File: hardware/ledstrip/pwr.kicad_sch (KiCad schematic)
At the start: 30 parts, among them J6 Header for STUSB4500 I2C, Q4 Q_PMOS, U6 STUSB4500QTR

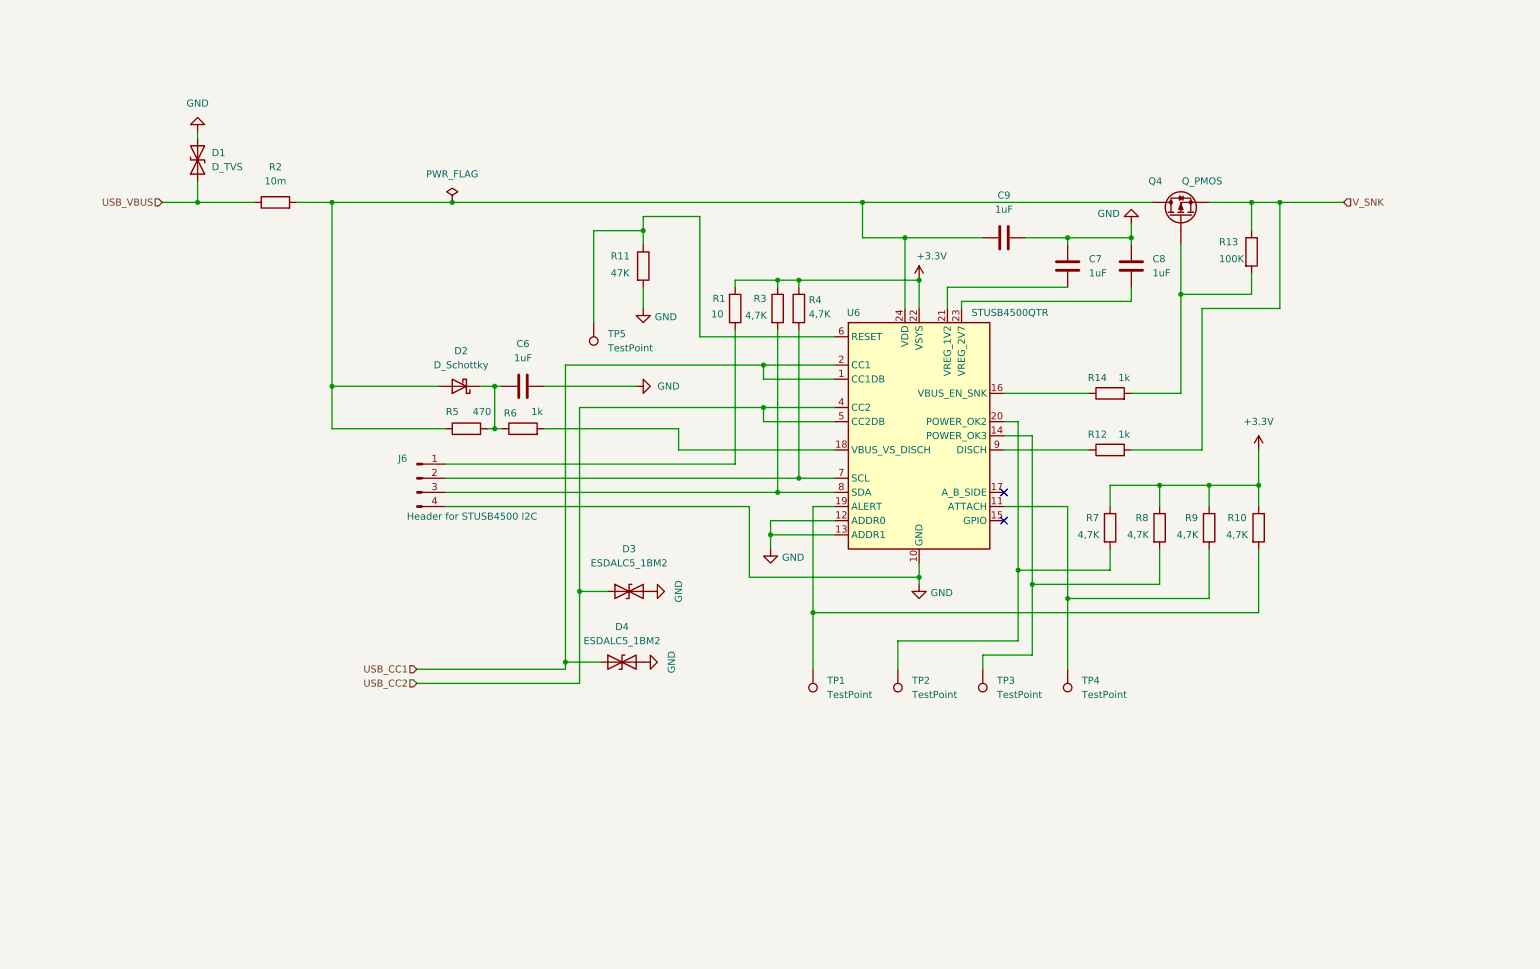
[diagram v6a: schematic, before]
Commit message: Add label on nodes.
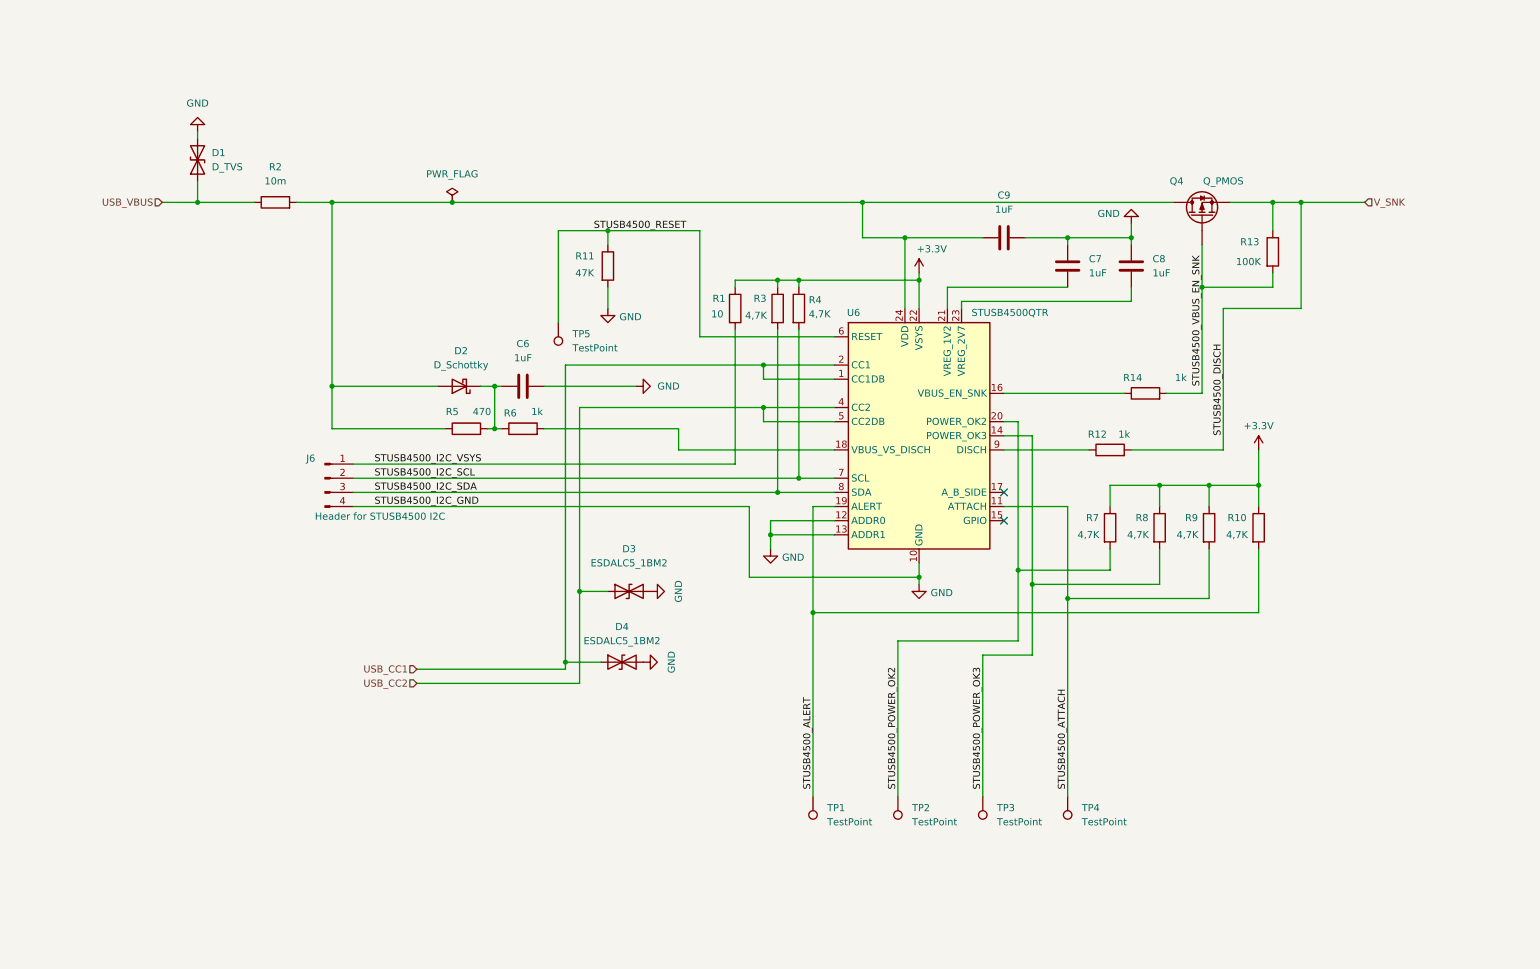
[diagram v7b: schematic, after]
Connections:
- net STUSB4500_POWER_OK3: now reaches R8.2, TP3.1, U6.14 (POWER_OK3)
- net STUSB4500_ATTACH: now reaches R9.2, TP4.1, U6.11 (ATTACH)
- net STUSB4500_I2C_VSYS: now reaches J6.1 (Pin_1), R1.2
- net STUSB4500_I2C_SCL: now reaches J6.2 (Pin_2), R4.2, U6.7 (SCL)
- net STUSB4500_I2C_SDA: now reaches J6.3 (Pin_3), R3.2, U6.8 (SDA)
- net STUSB4500_VBUS_EN_SNK: now reaches Q4.G, R13.2, R14.2
- net STUSB4500_RESET: now reaches R11.1, TP5.1, U6.6 (RESET)
- net STUSB4500_POWER_OK2: now reaches R7.2, TP2.1, U6.20 (POWER_OK2)
- net STUSB4500_ALERT: now reaches R10.2, TP1.1, U6.19 (ALERT)
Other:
- moved on the sheet: J6, Q4, R11, R13, R14, TP1, TP2, TP3, TP4, TP5

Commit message: Added a pull down to VSYS
(external powered if header connected, otherwise VSYS is tied to GND) in STUSB4500 integration.
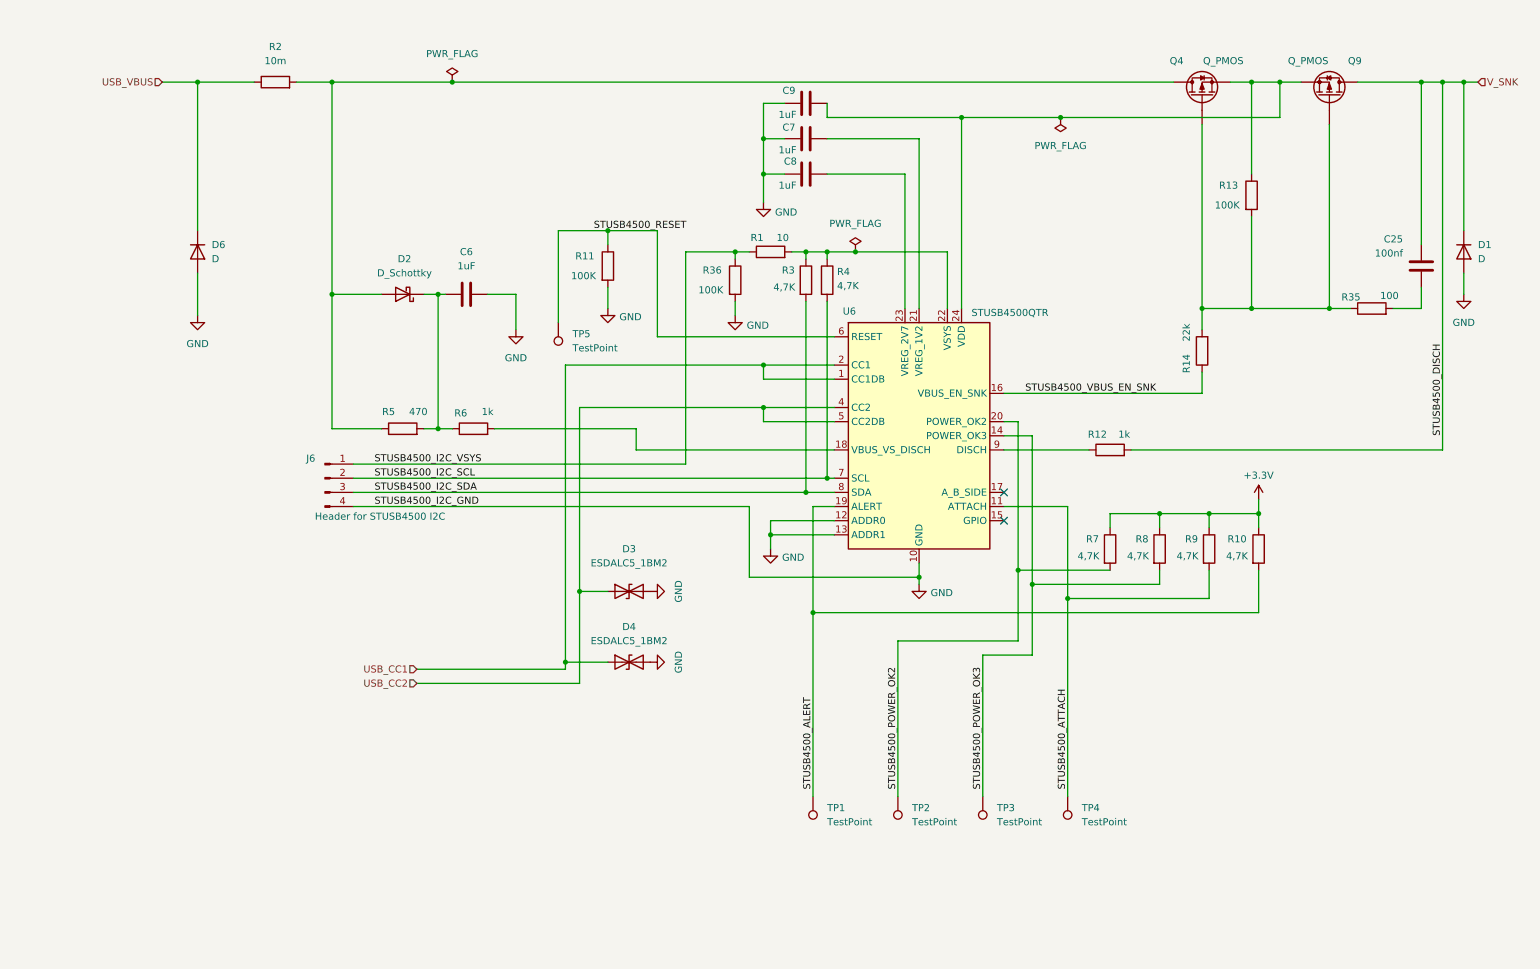
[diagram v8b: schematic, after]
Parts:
- removed D1: D_TVS, Diode_SMD:D_SMA, symbol Device:D_TVS
- added C25: 100nf, Capacitor_SMD:C_0603_1608Metric, symbol Device:C
- added D1: D, Diode_SMD:D_0603_1608Metric, symbol Device:D
- added D6: D, Diode_SMD:D_SMA, symbol Device:D
- added Q9: Q_PMOS, STL6P3LLH6:POWERFLAT_3P3X3P3_STM, symbol Device:Q_PMOS
- added R35: 100, Resistor_SMD:R_0805_2012Metric, symbol Device:R
- added R36: 100K, Resistor_SMD:R_0805_2012Metric, symbol Device:R
- R11: value 47K -> 100K; Distributor Link 1 https://www.mouser.fr/ProductDetail/Panasonic/ERA-6ARW473V?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 -> https://www.mouser.fr/ProductDetail/YAGEO/RT0805BRB07100KL?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; Distributor Link 2 https://www.digikey.com/en/products/detail/panasonic-electr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 -> https://www.digikey.com/en/products/detail/yageo/RT0805BRB0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
- R14: value 1k -> 22k; footprint Capacitor_SMD:C_0603_1608Metric -> Resistor_SMD:R_0805_2012Metric; Distributor Link 1 https://www.mouser.fr/ProductDetail/Vishay-Draloric/RCA0603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 -> https://www.mouser.fr/ProductDetail/Vishay-Beyschlag/MCU080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; Distributor Link 2 (none) -> https://www.digikey.com/en/products/detail/vishay/MCU08050C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
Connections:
- net +3.3V: no longer R1.1, R3.1, R4.1, U6.22 (VSYS)
- net GND: now also C9.1, D1.2 (A), D6.2 (A), R36.2; no longer C9.2
- net STUSB4500_I2C_VSYS: now also R1.1, R36.1; no longer R1.2
- net STUSB4500_VBUS_EN_SNK: now also R14.1, U6.16 (VBUS_EN_SNK); no longer Q4.G, R13.2, R14.2
- net USB_VBUS: now also D6.1 (K)
- net V_SNK: now also C25.1, D1.1 (K), Q9.D; no longer Q4.S, R13.1
- net at D2.2 (A), Q4.D, R2.2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: no longer C9.1, U6.24 (VDD)
- new net: Q4.G, Q9.G, R13.2, R14.2, R35.1
- new net: C25.2, R35.2
- new net: C9.2, Q4.S, Q9.S, R13.1, U6.24 (VDD)
- new net: R1.2, R3.1, R4.1, U6.22 (VSYS)
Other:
- moved on the sheet: C6, C7, C8, C9, D2, D4, Q4, R1, R10, R13, R14, R2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
